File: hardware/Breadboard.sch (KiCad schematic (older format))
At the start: 56 parts, among them J1 MP1-8, J2 PWRLED, J3 SWLED, Q1 BC547, Q2 BC547, Q3 LP0701N3-G, U1 A4988, U2 ULN2003, U3 MT3608, U4 PCF8574, U5 MCP23017, U6 PCF8574

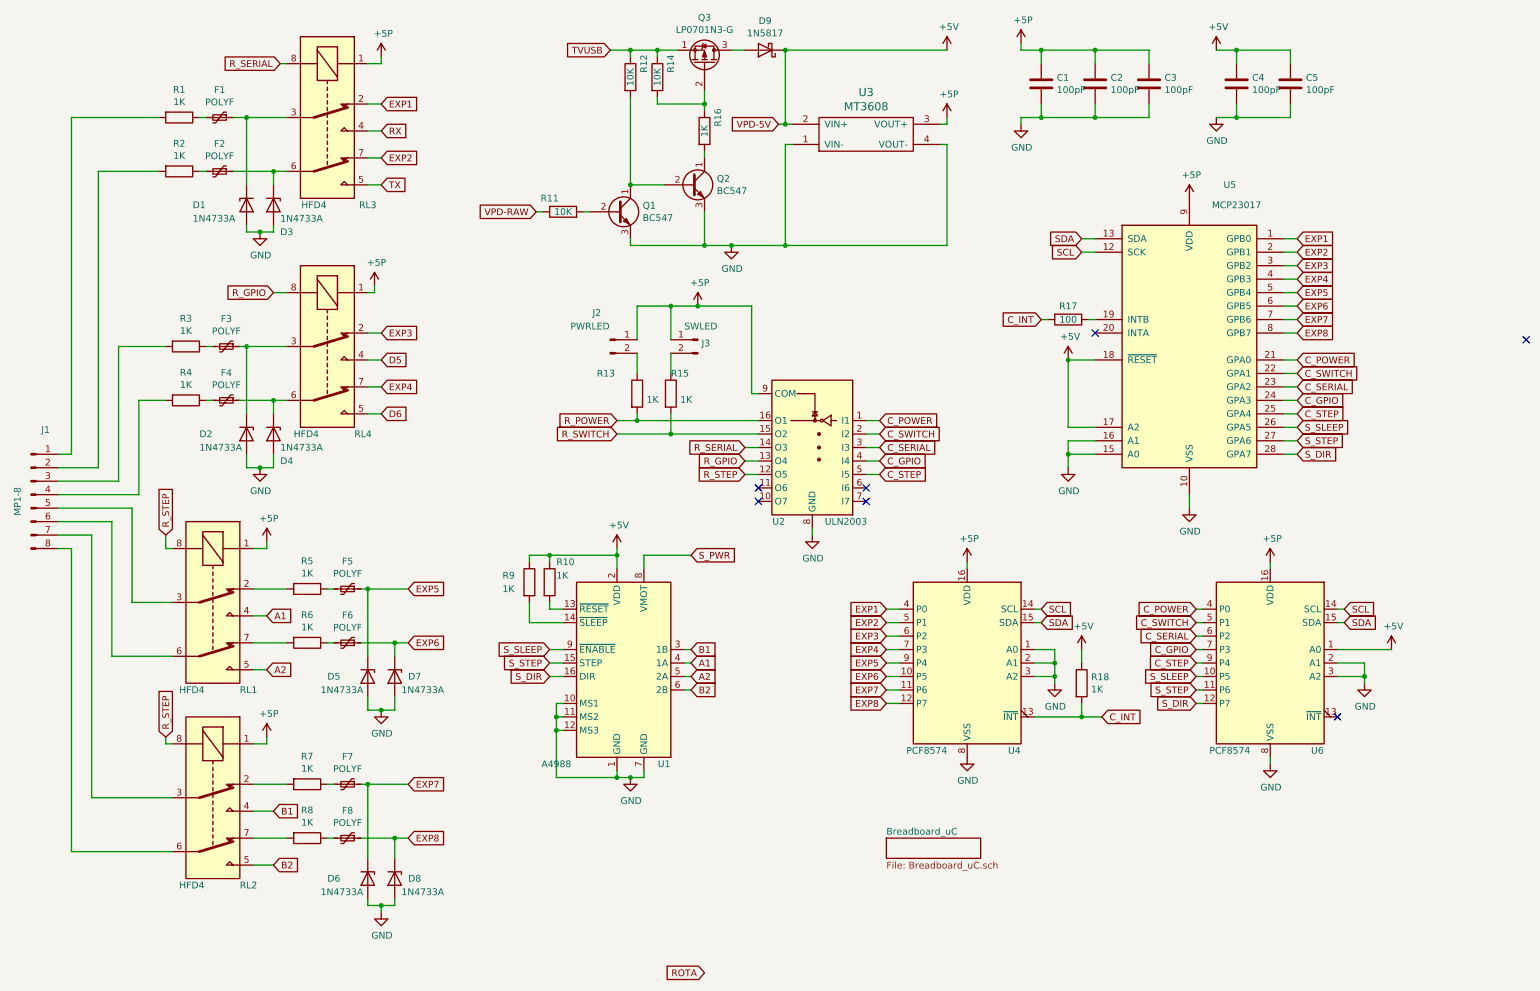
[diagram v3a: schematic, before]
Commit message: Cleanup main & interrupt driven I2C monitor
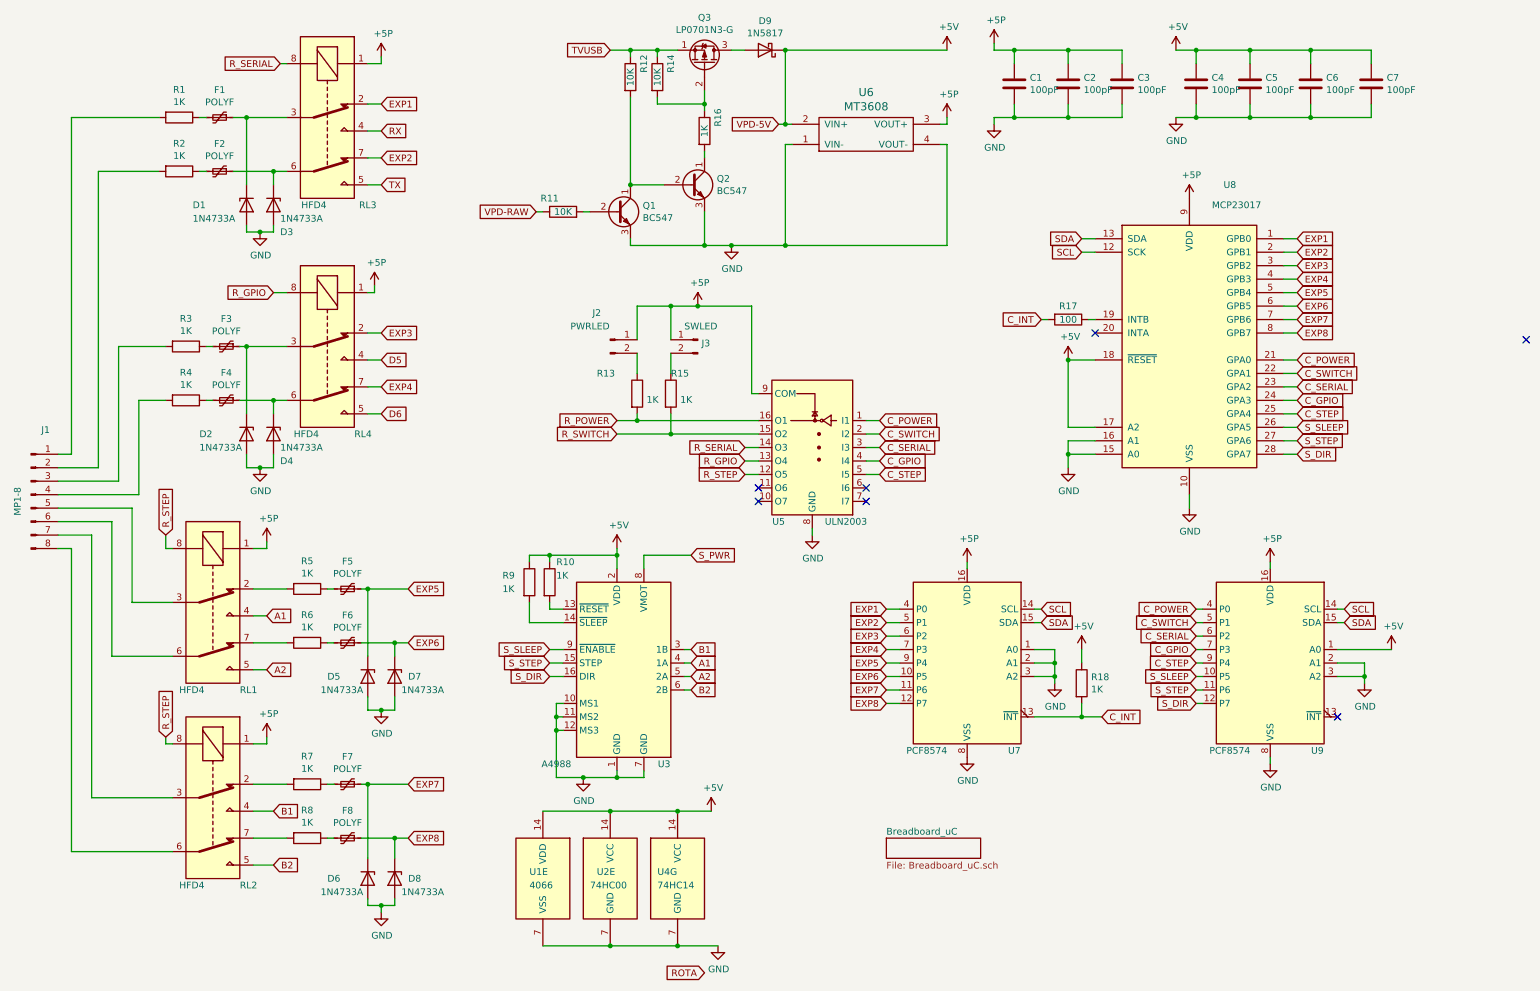
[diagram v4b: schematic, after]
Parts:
- added C6, C7: 100pF, Capacitor_THT:C_Axial_L3.8mm_D2.6mm_P7.50mm_Horizontal, symbol Device:C
- added U1: 4066, Package_DIP:DIP-14_W7.62mm, symbol 4xxx:4066
- added U2: 74HC00, Package_DIP:DIP-16_W7.62mm_LongPads, symbol 74xx:74HC00
- added U4: 74HC14, Package_DIP:DIP-16_W7.62mm_LongPads, symbol 74xx:74HC14
- renumbered U1 to U3, U2 to U5, U3 to U6, U4 to U7, U5 to U8, U6 to U9
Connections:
- net +5V: now also C6.1, C7.1, U1.14 (VDD), U2.14 (VCC), U4.14 (VCC)
- net GND: now also C6.2, C7.2, U1.7 (VSS), U2.7 (GND), U4.7 (GND)
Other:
- moved on the sheet: C1, C2, C3, C4, C5
